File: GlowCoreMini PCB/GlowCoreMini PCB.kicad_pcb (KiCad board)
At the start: 2 copper layers, 30 x 40 mm, 62 parts, among them P1 Solder_Pad, P10 Solder_Pad, P11 Solder_Pad, P12 Solder_Pad, P13 Solder_Pad, P14 Solder_Pad, P2 Solder_Pad, P3 Solder_Pad, P4 Solder_Pad, P5 Solder_Pad, P6 Solder_Pad, P7 Solder_Pad, P8 Solder_Pad, P9 Solder_Pad, SW1 TS24CA, SW2 TS24CA, SW3 TS24CA, SW4 TS24CA, U1 ESP32-WROOM-32E, U11 AO3400A, U12 CP2102-GMR, U14 UMH3N, U2 SN74LVC2T45DCUR, U3 MSM261D4030H1CPM, U4 SN74LVC1G373DBVR, U5 AP40P05, U6 SPX3819M5-L-3-3_TR, U7 SS54, U9 SN74LVC1G373DBVR

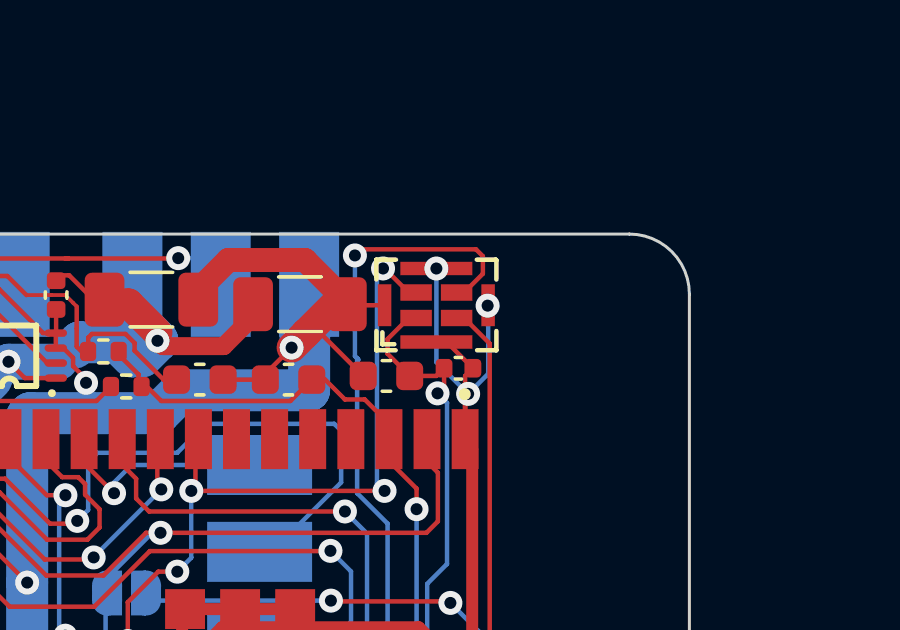
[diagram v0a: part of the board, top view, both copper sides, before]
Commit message: fixed via in ground pad
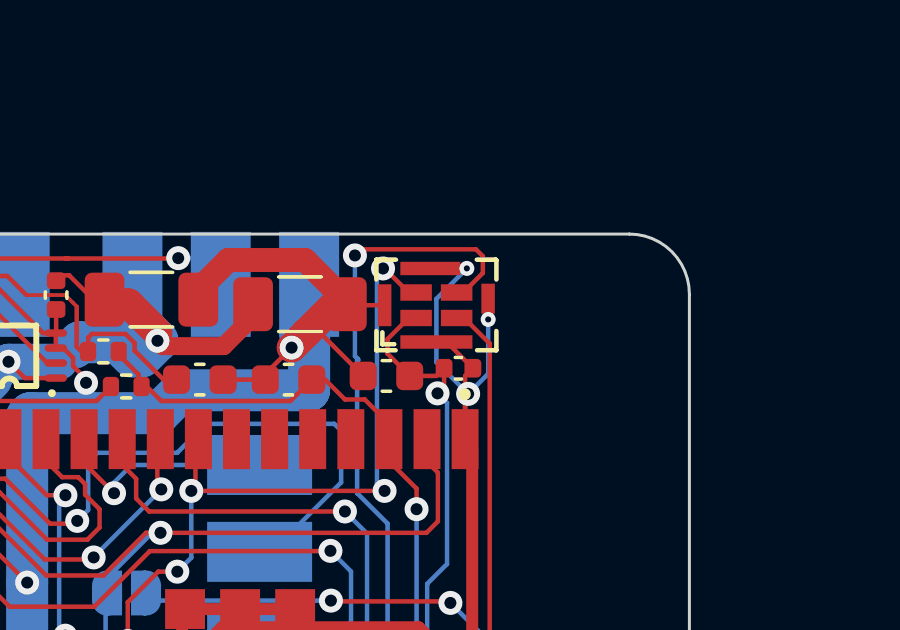
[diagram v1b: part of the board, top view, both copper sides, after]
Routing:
- net GND: track 263.4 -> 265.2 mm

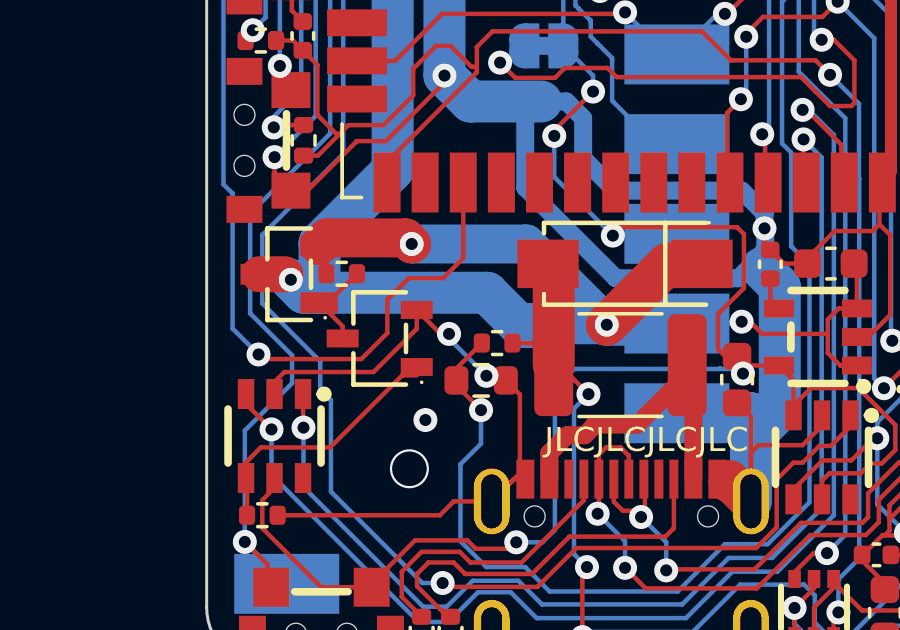
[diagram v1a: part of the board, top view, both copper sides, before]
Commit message: added status led
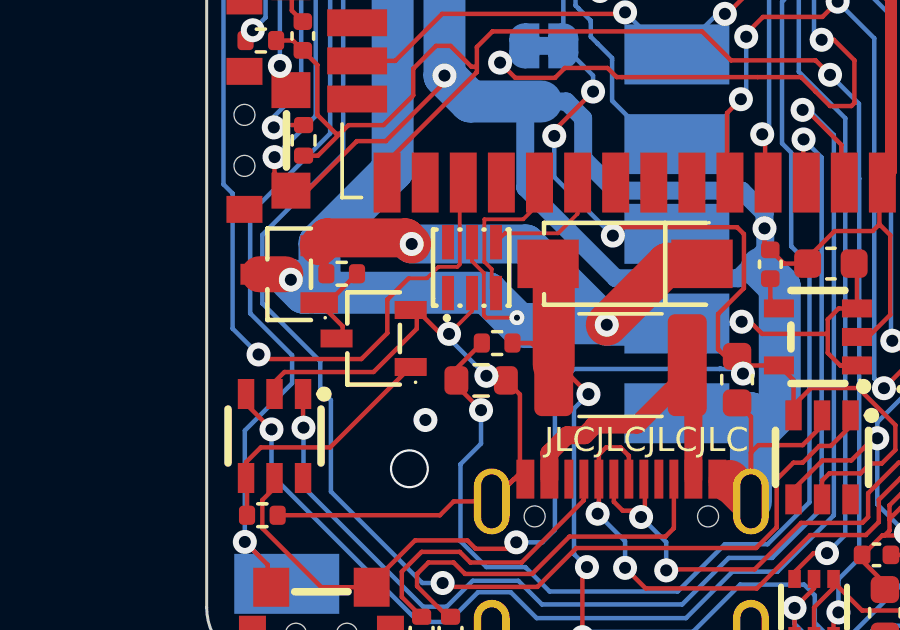
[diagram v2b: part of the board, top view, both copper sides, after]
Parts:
- added U8: SK9822-EC20, footprint:LED-SMD_6P-L2.0-W2.0-P0.80-TL, F.Cu at (91.5, 75.5)
- moved U11 0.20 mm to (88.3, 77.9)
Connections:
- U1 pad 29: IO5 -> IO5/STATUS LED DATA
- U1 pad 30: unconnected-(U1-Pad30) -> IO18/STATUS LED CLOCK
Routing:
- net IO5/STATUS LED DATA: track 0.00 -> 5.37 mm
- net IO18/STATUS LED CLOCK: track 0.00 -> 4.15 mm
- net 5V AFTER MOSFET: track 51.8 -> 55.6 mm, vias 3 -> 4
- net GND: track 265.2 -> 266.9 mm
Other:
- board text added: "Status LED: DATA: IO5 CLK: IO18"

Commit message: continued redesign of pcb
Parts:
- removed C4: 0.1uF, Capacitor_SMD:C_0402_1005Metric
- removed H1, H2: MountingHole_Pad, MountingHole:MountingHole_2.2mm_M2_ISO7380
- removed JP1: SolderJumper_2_Bridged, Jumper:SolderJumper-2_P1.3mm_Bridged_RoundedPad1.0x1.5mm
- removed JP2, JP4: SolderJumper_2_Open, Jumper:SolderJumper-2_P1.3mm_Open_RoundedPad1.0x1.5mm
- removed SW4: TS24CA, footprint:SW-SMD_TS24CA
- added C15: 10uF, Capacitor_SMD:C_0603_1608Metric, F.Cu at (88.0, 54.6)
- added C16: 0.1uF, Capacitor_SMD:C_0402_1005Metric, F.Cu at (86.1, 65.8)
- added C17: 10uF, Capacitor_SMD:C_0603_1608Metric, F.Cu at (86.1, 84.2)
- added C18: 10nF, Capacitor_SMD:C_0402_1005Metric, F.Cu at (86.4, 79.5)
- added C19: 10uF, Capacitor_SMD:C_0603_1608Metric, F.Cu at (86.3, 77.8)
- added C21: 220uF, Capacitor_SMD:C_1206_3216Metric, F.Cu at (96.7, 72.7)
- added G***: LOGO, LOGO, B.Cu at (98.0, 68.9)
- added L1: WPN4020H1R0MT, footprint:IND-SMD_L4.0-W4.0_SLW40XX, F.Cu at (99.7, 78.0)
- added P15: Solder_Pad, footprint:Solder pad, B.Cu at (99.2, 72.3)
- added P16: Solder_Pad, footprint:Solder pad, B.Cu at (95.1, 69.9)
- added P17: Solder_Pad, footprint:Solder pad, B.Cu at (99.3, 64.4)
- added P18: Solder_Pad, footprint:Solder pad, B.Cu at (99.2, 69.7)
- added P19: Solder_Pad, footprint:Solder pad, B.Cu at (95.1, 54.5)
- added P20: Solder_Pad, footprint:Solder pad, B.Cu at (99.2, 67.1)
- added P21: Solder_Pad, footprint:Solder pad, B.Cu at (95.2, 51.9)
- added P22: Solder_Pad, footprint:Solder pad, B.Cu at (99.3, 51.9)
- added R10: 10K, Resistor_SMD:R_0402_1005Metric, F.Cu at (105.1, 72.5)
- added R11: 10K, Resistor_SMD:R_0402_1005Metric, F.Cu at (104.2, 72.5)
- added R16: 100K, Resistor_SMD:R_0402_1005Metric, F.Cu at (118.8, 76.7)
- added R17: 5.1K, Resistor_SMD:R_0402_1005Metric, F.Cu at (85.8, 57.8)
- added R18: 33K, Resistor_SMD:R_0402_1005Metric, F.Cu at (87.6, 76.1)
- added R19: 100K, Resistor_SMD:R_0402_1005Metric, F.Cu at (85.5, 76.5)
- added R2: 10K, Resistor_SMD:R_0402_1005Metric, F.Cu at (89.3, 68.9)
- added R20: 10K, Resistor_SMD:R_0402_1005Metric, F.Cu at (87.7, 51.7)
- added R21: 100K, Resistor_SMD:R_0402_1005Metric, F.Cu at (92.9, 75.6)
- added R22: 100K, Resistor_SMD:R_0402_1005Metric, F.Cu at (92.9, 78.8)
- added R23: 5.1K, Resistor_SMD:R_0402_1005Metric, F.Cu at (103.7, 86.3)
- added R24: 5.1K, Resistor_SMD:R_0402_1005Metric, F.Cu at (103.7, 85.3)
- added REF1: RT9471DGQW, footprint:RT9471_vias_in_pad, F.Cu at (104.6, 76.3)
- added U10: LSM6DS3TR-C, footprint:LGA-14_L3.0-W2.5-P0.50-TL, F.Cu at (88.1, 65.8)
- added U13: SK9822-EC20, footprint:LED-SMD_6P-L2.0-W2.0-P0.80-TL, F.Cu at (96.8, 68.5)
- added U15: AP40P05, footprint:SOT-23-3_L2.9-W1.3-P1.90-LS2.4-BR, F.Cu at (94.7, 78.8)
- C1: value 0.1uF -> 1uF
- C10: value 4.7uF -> 0.1uF; footprint Capacitor_SMD:C_0603_1608Metric -> Capacitor_SMD:C_0402_1005Metric
- C12: value 10uF -> 1uF; footprint Capacitor_SMD:C_0603_1608Metric -> Capacitor_SMD:C_0402_1005Metric
- C13: value 1uF -> 0.1uF
- C14: value 10uF -> 0.1uF; footprint Capacitor_SMD:C_0603_1608Metric -> Capacitor_SMD:C_0402_1005Metric
- C2: value 0.1uF -> 10uF; footprint Capacitor_SMD:C_0402_1005Metric -> Capacitor_SMD:C_0603_1608Metric
- C5: value 10uF -> 4.7uF; footprint Capacitor_SMD:C_0603_1608Metric -> Capacitor_SMD:C_0402_1005Metric
- C6: value 10uF -> 47nF; footprint Capacitor_SMD:C_0603_1608Metric -> Capacitor_SMD:C_0402_1005Metric
- C7, C9: value 220uF -> 10uF; footprint Capacitor_SMD:C_1206_3216Metric_Pad1.33x1.80mm_HandSolder -> Capacitor_SMD:C_0603_1608Metric
- C8: value 10nF -> 10uF; footprint Capacitor_SMD:C_0402_1005Metric -> Capacitor_SMD:C_0603_1608Metric
- R1: value 62 -> 100K
- R12, R13: value 220 -> 100K
- R14, R15: value 10K -> 62
- R7, R8: value 5.1K -> 10K
- U1: value ESP32-WROOM-32E -> SN74LVC1G373DBVR; footprint footprint:WIFI-SMD_ESP32-WROOM-32E -> footprint:SOT-23-6_L2.9-W1.6-P0.95-LS2.8-BR
- U11: value AO3400A -> MSM261D4030H1CPM; footprint footprint:SOT-23-3_L2.9-W1.6-P1.90-LS2.8-BR -> footprint:MIC-SMD_8P-L4.0-W3.0_ZTS6231
- U12: value CP2102-GMR -> SPX3819M5-L-3-3_TR; footprint footprint:QFN-28_L5.0-W5.0-P0.50-BL-EP -> footprint:SOT-23-5_L3.0-W1.7-P0.95-LS2.8-BR
- U14: value UMH3N -> AP40P05; footprint footprint:SC-70-6_L2.2-W1.3-P0.65-LS2.1-BR -> footprint:SOT-23-3_L2.9-W1.3-P1.90-LS2.4-BR
- U2: value SN74LVC2T45DCUR -> ESP32-S3-MINI-1-N8; footprint footprint:VSSOP-8_L2.4-W2.1-P0.50-LS3.2-BR -> footprint:ESP32-S3-MINI-1-N8
- U3: value MSM261D4030H1CPM -> PTVSHC3N12VU; footprint footprint:MIC-SMD_8P-L3.0-W4.0-P0.85-BL -> footprint:DFN-3_L2.0-W2.0-P1.30-BR
- U4: value SN74LVC1G373DBVR -> AP40P05; footprint footprint:SOT-23-6_L2.9-W1.6-P0.95-LS2.8-BR -> footprint:SOT-23-3_L2.9-W1.3-P1.90-LS2.4-BR
- U6: value SPX3819M5-L-3-3_TR -> AO3400A; footprint footprint:SOT-23-5_L3.0-W1.7-P0.95-LS2.8-BR -> footprint:SOT-23-3_L2.9-W1.6-P1.90-LS2.8-BR
- U7: value SS54 -> 74LVC2G04DW-7; footprint footprint:SMA_L4.4-W2.8-LS5.4-RD -> footprint:SOT-363_L2.0-W1.3-P0.65-LS2.1-BR
- U8: value SK9822-EC20 -> AP40P05; footprint footprint:LED-SMD_6P-L2.0-W2.0-P0.80-TL -> footprint:SOT-23-3_L2.9-W1.3-P1.90-LS2.4-BR
- U9: value SN74LVC1G373DBVR -> SN74LVC2T45DCUR; footprint footprint:SOT-23-6_L2.9-W1.6-P0.95-LS2.8-BR -> footprint:VSSOP-8_L2.4-W2.1-P0.50-LS3.2-BR
- moved SW2 38.7 mm to (107.5, 87.8), turned to 180 degrees
- moved R9 37.6 mm to (118.8, 77.7)
- moved C2 33.2 mm to (106.2, 80.5)
- moved C1 30.7 mm to (107.8, 76.9)
- moved R1 28.9 mm to (107.4, 73.6), turned to 0 degrees
- moved U3 28.1 mm to (108.6, 78.9), turned to 0 degrees
- moved C11 27.7 mm to (85.2, 65.8), turned to -90 degrees
- moved C5 26.5 mm to (104.8, 79.9), turned to -90 degrees
- moved P1 26.0 mm to (95.1, 76.5), turned to -90 degrees
- moved P13 26.0 mm to (95.2, 62.1), turned to 90 degrees
- moved P2 26.0 mm to (99.2, 76.5), turned to -90 degrees
- moved C9 23.5 mm to (100.2, 73.9), turned to -90 degrees
- moved P3 22.5 mm to (95.1, 72.5), turned to -90 degrees
- moved U12 22.5 mm to (86.4, 81.5)
- moved C7 21.8 mm to (101.7, 72.9), turned to -90 degrees
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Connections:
- C1 pad 1: 5V AFTER MOSFET -> -BATT
- C1 pad 2: GND -> VBUS
- C10 pad 1: GND -> 5V AFTER MOSFET
- C10 pad 2: Net-(C10-Pad2) -> -BATT
- C11 pad 1: Net-(C10-Pad2) -> 3.3V AFTER MOSFET
- C11 pad 2: GND -> -BATT
- C12 pad 1: GND -> -BATT
- C13 pad 1: IO0 -> -BATT
- C13 pad 2: GND -> 3.3V AFTER MOSFET
- C14 pad 1: GND -> 3.3V AFTER MOSFET
- C14 pad 2: +3V3 -> -BATT
- C2 pad 1: +3V3 -> -BATT
- C2 pad 2: GND -> Net-(REF1-PMID)
- C3 pad 1: +3V3 -> -BATT
- C3 pad 2: GND -> +3V3
- C5 pad 1: GND -> REGN
- C5 pad 2: Net-(C4-Pad2) -> -BATT
- C6 pad 1: GND -> Net-(REF1-BTST)
- C6 pad 2: +5V -> Net-(C6-Pad2)
- C7 pad 1: 5V AFTER MOSFET -> -BATT
- C7 pad 2: GND -> +BATT
- C8 pad 1: GND -> -BATT
- C8 pad 2: Net-(C8-Pad2) -> +5V
- C9 pad 1: 5V AFTER MOSFET -> -BATT
- C9 pad 2: GND -> +5V
- F1 pad 1: Net-(F1-Pad1) -> +5V
- F1 pad 2: VBUS -> Net-(F1-Pad2)
- P1 pad 1: 5V AFTER MOSFET -> Net-(U8-D)
- P10 pad 1: +3V3 -> 3.3V AFTER MOSFET
- P11 pad 1: IO32/SD -> EN
- P12 pad 1: IO27 -> LED1 DATA OUT
- P13 pad 1: IO33/MAINBUTTON -> IO1/POWERBUTTON
- P14 pad 1: IO26 -> IO3/ACTIONBUTTON
- P2 pad 1: LED1 DATA OUT -> -BATT
- P3 pad 1: GND -> 5V AFTER MOSFET
- P4 pad 1: +5V -> Net-(F1-Pad2)
- P5 pad 1: GND -> -BATT
- P6 pad 1: IO12/TDI -> IO36/SPI SCK
- P7 pad 1: IO13/TCK -> IO35/SPI MO
- P8 pad 1: IO14/SCK/TMS -> TXD0
- P9 pad 1: IO15/WS/TDO -> RXD0
- R1 pad 1: Net-(R1-Pad1) -> IO47/BATT IC EN
- R1 pad 2: LED1 DATA OUT -> -BATT
- R12 pad 1: Net-(R12-Pad1) -> Net-(U14-G)
- R12 pad 2: EN -> +3V3
- R13 pad 1: Net-(R13-Pad1) -> -BATT
- R13 pad 2: IO0 -> Net-(U8-G)
- R14 pad 1: EN -> Net-(U9-A1)
- R14 pad 2: +3V3 -> LED1 DATA OUT
- R15 pad 1: IO0 -> Net-(U9-A2)
- R15 pad 2: +3V3 -> LED2 DATA OUT
- R3 pad 1: IO25/VBUS -> IO7/VBUS
- R4 pad 1: GND -> -BATT
- R4 pad 2: IO25/VBUS -> IO7/VBUS
- R5 pad 1: Net-(R5-Pad1) -> Net-(U14-G)
- R6 pad 1: GND -> -BATT
- R6 pad 2: Net-(R6-Pad2) -> Net-(U1-Q)
- R7 pad 1: GND -> +3V3
- R7 pad 2: USB-C CC1 -> IO9/I2C SCL
- R8 pad 1: GND -> +3V3
- R8 pad 2: USB-C CC2 -> IO10/I2C GRYO INT
- R9 pad 1: Net-(R9-Pad1) -> Net-(U7-1A)
- R9 pad 2: GND -> +3V3
- SW1 pad 3: +3V3 -> -BATT
- SW1 pad 4: IO33/MAINBUTTON -> Net-(U7-1A)
- SW2 pad 3: Net-(R9-Pad1) -> -BATT
- SW2 pad 4: +3V3 -> IO0/BOOT
- SW3 pad 3: GND -> -BATT
- SW3 pad 4: Net-(R12-Pad1) -> EN
- U1 pad 1: GND -> IO15/LED LETCH EN
- U1 pad 2: +3V3 -> -BATT
- U1 pad 3: EN -> IO16/POWERMOSFETS
- U1 pad 4: unconnected-(U1-Pad4) -> Net-(U1-Q)
- U1 pad 5: unconnected-(U1-Pad5) -> +3V3
- U11 pad 1: Net-(R6-Pad2) -> 3.3V AFTER MOSFET
- U11 pad 2: GND -> IO12/I2S WS
- U11 pad 3: Net-(R5-Pad1) -> IO13/I2S SCK
- U12 pad 1: unconnected-(U12-Pad1) -> +5V
- U12 pad 2: unconnected-(U12-Pad2) -> -BATT
- U12 pad 3: GND -> +5V
- U12 pad 4: USB-C DATA+ -> Net-(U12-BYP)
- U12 pad 5: USB-C DATA- -> +3V3
- U14 pad 1: RTS -> Net-(U14-G)
- U14 pad 2: DTR -> +5V
- U14 pad 3: IO0 -> 5V AFTER MOSFET
- U2 pad 1: 5V AFTER MOSFET -> -BATT
- U2 pad 2: Net-(R1-Pad1) -> -BATT
- U2 pad 3: GND -> +3V3
- U2 pad 4: GND -> IO0/BOOT
- U2 pad 5: GND -> IO1/POWERBUTTON
- U2 pad 6: GND -> IO2/BATT VOLT
- U2 pad 7: IO16/LED1 -> IO3/ACTIONBUTTON
- U2 pad 8: +3V3 -> unconnected-(U2-IO4-Pad8)
- U3 pad 1: Net-(C4-Pad2) -> -BATT
- U3 pad 2: IO15/WS/TDO -> -BATT
- U3 pad 3: IO14/SCK/TMS -> VBUS
- U4 pad 1: IO22/LED LETCH EN -> Net-(U14-G)
- U4 pad 2: GND -> +5V
- U4 pad 3: IO23/POWERMOSFETS -> 5V AFTER MOSFET
- U5 pad 1: Net-(R5-Pad1) -> Net-(U14-G)
- U5 pad 2: +5V -> +3V3
- U5 pad 3: 5V AFTER MOSFET -> 3.3V AFTER MOSFET
- U6 pad 1: +5V -> Net-(U1-Q)
- U6 pad 2: GND -> -BATT
- U6 pad 3: +5V -> Net-(U14-G)
- U7 pad 1: +5V -> Net-(U7-1A)
- U7 pad 2: VBUS -> -BATT
- U8 pad 1: unconnected-(U8-Pad1) -> Net-(U8-G)
- U8 pad 2: GND -> +BATT
- U8 pad 3: IO5/STATUS LED DATA -> Net-(U8-D)
- U9 pad 1: Net-(R9-Pad1) -> 5V AFTER MOSFET
- U9 pad 2: GND -> Net-(U9-A1)
- U9 pad 3: +3V3 -> Net-(U9-A2)
- U9 pad 4: Net-(C10-Pad2) -> -BATT
- U9 pad 5: +3V3 -> -BATT
- U9 pad 6: unconnected-(U9-Pad6) -> IO41/LED2
- USB1 pad A1B12: GND -> -BATT
- USB1 pad A4B9: Net-(F1-Pad1) -> VBUS
- USB1 pad A6: USB-C DATA+ -> USB D+
- USB1 pad A7: USB-C DATA- -> USB D-
- USB1 pad B1A12: GND -> -BATT
- USB1 pad B4A9: Net-(F1-Pad1) -> VBUS
- USB1 pad B6: USB-C DATA+ -> USB D+
- USB1 pad B7: USB-C DATA- -> USB D-
- USB1 pad SHELL: GND -> -BATT
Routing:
- net GND: track 266.9 -> 0.00 mm, vias 18 -> 0
- net +3V3: track 133.7 -> 0.00 mm, vias 10 -> 0
- net Net-(R9-Pad1): track 64.5 -> 0.00 mm, vias 2 -> 0
- net IO25/VBUS: track 56.5 -> 0.00 mm, vias 2 -> 0
- net 5V AFTER MOSFET: track 55.6 -> 0.00 mm, vias 4 -> 0
- net IO0: track 50.3 -> 0.00 mm, vias 2 -> 0
- net IO14/SCK/TMS: track 48.5 -> 0.00 mm, vias 6 -> 0
- net IO33/MAINBUTTON: track 47.0 -> 0.00 mm, vias 4 -> 0
- net Net-(C10-Pad2): track 44.7 -> 0.00 mm, vias 4 -> 0
- net EN: track 43.6 -> 0.00 mm, vias 2 -> 0
- net IO23/POWERMOSFETS: track 43.1 -> 0.00 mm, vias 2 -> 0
- net IO16/LED1: track 41.2 -> 0.00 mm, vias 2 -> 0
- net IO22/LED LETCH EN: track 38.0 -> 0.00 mm, vias 2 -> 0
- net Net-(C4-Pad2): track 36.2 -> 0.00 mm, vias 3 -> 0
- net IO15/WS/TDO: track 35.5 -> 0.00 mm, vias 4 -> 0
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- added copper zone on In2.Cu, net +5V
- added copper zone on In1.Cu, net -BATT
- added copper zone on In2.Cu, net 5V AFTER MOSFET
- removed copper zone on B.Cu, net GND
- removed copper zone on F.Cu, net GND
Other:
- outline, holes or cut-outs redrawn
- copper layers 2 -> 4
- board text removed: "200mA max"
- board text removed: "2A max"
- board text removed: "3.3V OUT"
- board text removed: "3A max"
- board text removed: "5V"
- board text removed: "5V IN"
- board text removed: "BOOT"
- board text removed: "G"
- board text removed: "GND"
- board text removed: "GlowCore Mini v2.0"
- board text removed: "IO12/TDI"
- board text removed: "IO13/TCK"
- board text removed: "IO14/SCK/TMS"
- board text removed: "IO15/WS/TDO"
- board text removed: "IO16"
- board text removed: "IO26"
- board text removed: "IO27"
- board text removed: "IO32/SD"
- board text removed: "IO33/ B1"
- board text removed: "LEDs always on"
- board text removed: "RESET"
- board text removed: "SERIAL"
- board text removed: "Serial always on"
- board text removed: "Status LED: DATA: IO5 CLK: IO18"
- board text removed: "https:// bit.ly/ 3GnbIkg"
- board text removed: "microphone on"

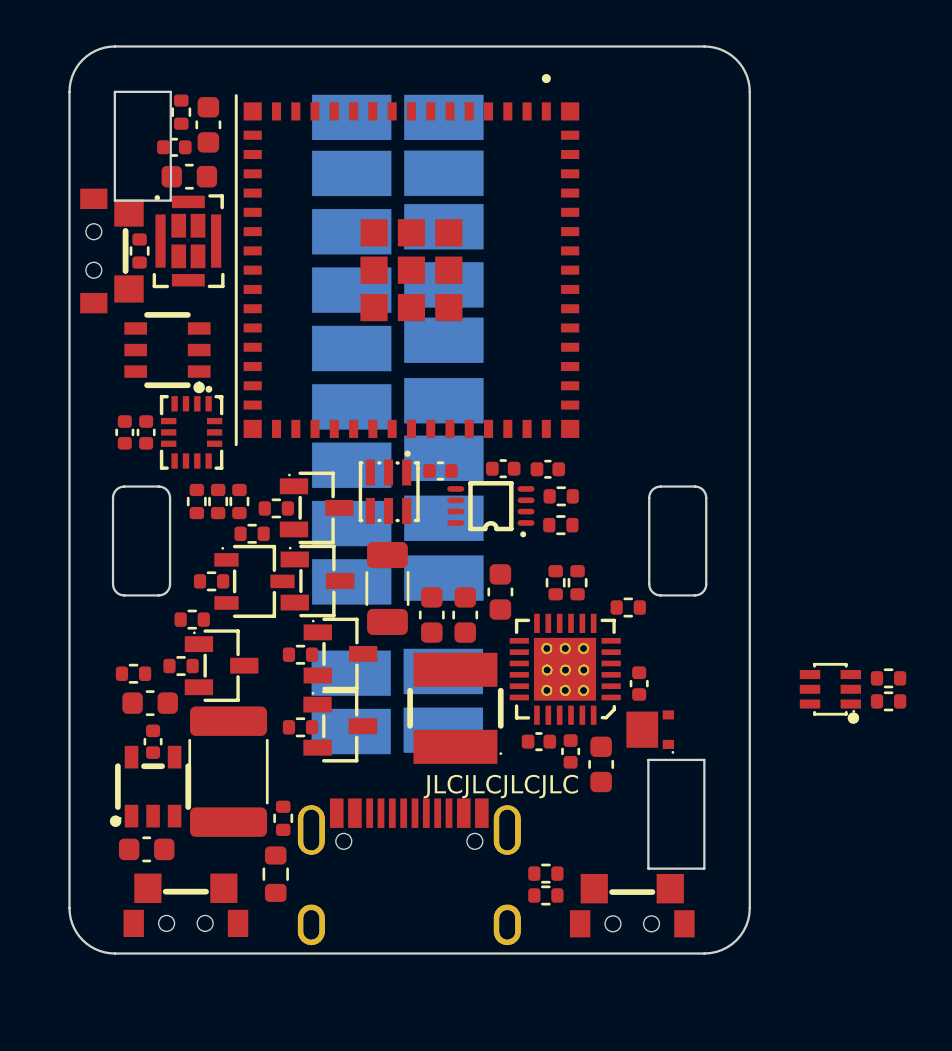
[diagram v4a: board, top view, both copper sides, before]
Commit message: split up schematic
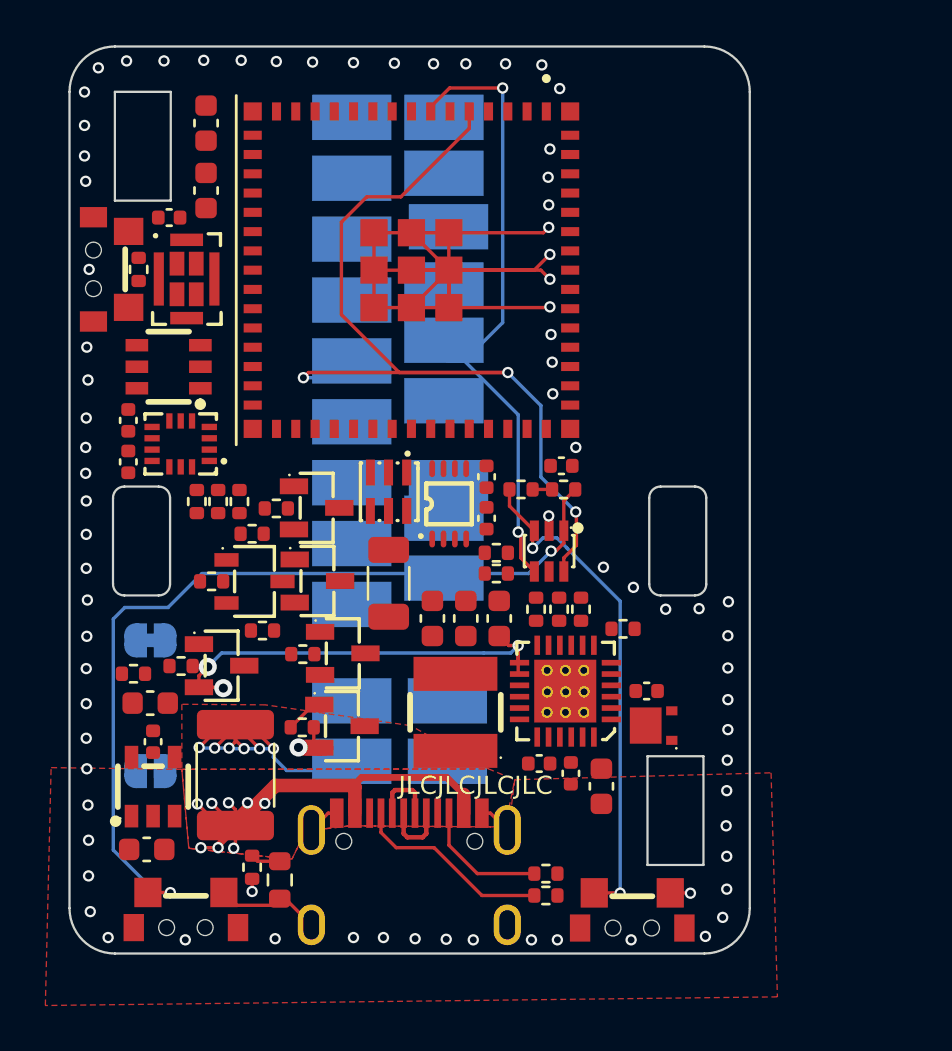
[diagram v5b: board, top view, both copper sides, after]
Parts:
- removed G***: LOGO, LOGO
- added JP1: SolderJumper_2_Open, Jumper:SolderJumper-2_P1.3mm_Open_RoundedPad1.0x1.5mm, B.Cu at (86.3, 80.8)
- added JP2: SolderJumper_2_Bridged, Jumper:SolderJumper-2_P1.3mm_Bridged_RoundedPad1.0x1.5mm, B.Cu at (86.3, 75.0)
- moved R20 26.9 mm to (103.3, 73.6), turned to -90 degrees
- moved R16 18.2 mm to (102.6, 68.4)
- moved R9 17.1 mm to (104.5, 68.4), turned to 180 degrees
- moved U7 13.8 mm to (103.9, 71.1), turned to 90 degrees
- moved R15 3.79 mm to (101.5, 71.1)
- moved R14 3.56 mm to (101.5, 72.1)
- moved R13 3.14 mm to (91.2, 74.6)
- moved C13 3.11 mm to (87.1, 56.4)
- moved R3 2.56 mm to (90.8, 85.0), turned to -90 degrees
- moved C10 2.31 mm to (101.1, 69.6), turned to -90 degrees
- moved C14 2.05 mm to (101.1, 67.8), turned to -90 degrees
- moved U9 1.85 mm to (99.5, 69.0), turned to -90 degrees
- moved U11 1.67 mm to (87.9, 59.1)
- moved P2 1.38 mm to (99.3, 77.8)
- moved P5 1.38 mm to (99.3, 80.4)
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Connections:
- C17 pad 2: +5V -> VSYS
- C21 pad 1: +5V -> VBUS
- C8 pad 2: +5V -> Net-(JP2-A)
- C9 pad 2: +5V -> Net-(JP2-A)
- F1 pad 1: +5V -> Net-(JP1-A)
- F1 pad 2: Net-(F1-Pad2) -> VBUS
- L1 pad 2: +5V -> Net-(JP2-A)
- P4 pad 1: Net-(F1-Pad2) -> VBUS
- R21 pad 2: +5V -> VBUS
- R22 pad 2: +5V -> VBUS
- R5 pad 2: +5V -> VBUS
- REF1 pad 15: +5V -> Net-(JP2-A)
- REF1 pad 16: +5V -> Net-(JP2-A)
- U12 pad 1: +5V -> VSYS
- U12 pad 3: +5V -> VSYS
- U14 pad 2: +5V -> VBUS
- U15 pad 2: +5V -> VBUS
- U4 pad 2: +5V -> VBUS
- USB1 pad A4B9: VBUS -> Net-(JP1-A)
- USB1 pad B4A9: VBUS -> Net-(JP1-A)
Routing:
- net -BATT: track 0.00 -> 51.9 mm, vias 0 -> 75
- net IO1/POWERBUTTON: track 0.00 -> 42.4 mm, vias 0 -> 3
- net Net-(U7-1A): track 0.00 -> 38.3 mm, vias 0 -> 2
- net IO3/ACTIONBUTTON: track 0.00 -> 27.9 mm, vias 0 -> 2
- net Net-(JP1-A): track 0.00 -> 25.2 mm, vias 0 -> 8
- net IO0/BOOT: track 0.00 -> 22.3 mm, vias 0 -> 2
- net +BATT: track 0.00 -> 20.0 mm, vias 0 -> 3
- net VBUS: track 0.00 -> 19.7 mm, vias 0 -> 8
- net USB-C CC1: track 0.00 -> 8.76 mm
- net USB-C CC2: track 0.00 -> 5.69 mm
- net USB D+: track 0.00 -> 2.94 mm
- net USB D-: track 0.00 -> 2.90 mm
- net Net-(U14-G): track 0.00 -> 1.68 mm
- net IO7/VBUS: track 0.00 -> 1.32 mm
- net +3V3: track 0.00 -> 0.86 mm
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- added copper zone on F.Cu, net -BATT
- added copper zone on F.Cu, net Net-(JP1-A)
- added copper zone on F.Cu, net VBUS
- added copper zone on In2.Cu, net VBUS
- removed copper zone on In2.Cu, net +5V
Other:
- outline, holes or cut-outs redrawn
- board text added: "AB"
- board text added: "EN"
- board text added: "GlowCore Mini v3.1"
- board text added: "PB"
- board text added: "bit.ly/ 3l6y4On"
- board text added: "locked"

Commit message: updated pcb design
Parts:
- moved P15 1.19 mm to (99.4, 73.5)
- moved P18 1.13 mm to (99.3, 70.8)
- moved P17 0.95 mm to (99.4, 65.3)
- moved P14 0.92 mm to (99.4, 62.6)
- moved P9 0.69 mm to (99.2, 60.1)
- moved P7 0.59 mm to (99.2, 57.4)
- moved R10 0.49 mm to (105.8, 73.6), turned to 180 degrees
- moved P6 0.23 mm to (99.3, 54.6)
- moved C4 0.10 mm to (96.8, 72.6)
- moved JP2 0.05 mm to (86.3, 75.1)
- turned C13 to 180 degrees
- turned C14 to 90 degrees
- turned R17 to 90 degrees
- turned R22 to 180 degrees
- renumbered C21 to C4, U5 to U15, U15 to U5
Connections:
- R22 pad 1: Net-(U14-G) -> VBUS
- R22 pad 2: VBUS -> Net-(U14-G)
- U2 pad 37: IO41/LED2 -> IO41/LED1
- U2 pad 38: IO42/LED1 -> IO42/LED2
- U9 pad 6: IO41/LED2 -> IO42/LED2
- U9 pad 7: IO42/LED1 -> IO41/LED1
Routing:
- net +3V3: track 0.86 -> 101.5 mm, vias 0 -> 14
- net 3.3V AFTER MOSFET: track 0.00 -> 65.9 mm, vias 0 -> 7
- net IO8/I2C SDA: track 0.00 -> 60.5 mm, vias 0 -> 4
- net IO9/I2C SCL: track 0.00 -> 53.3 mm, vias 0 -> 5
- net IO7/VBUS: track 1.32 -> 53.5 mm, vias 0 -> 2
- net -BATT: track 51.9 -> 98.6 mm, vias 75 -> 99
- net IO2/BATT VOLT: track 0.00 -> 43.1 mm, vias 0 -> 2
- net IO11/I2C BATT IC INT: track 0.00 -> 41.9 mm, vias 0 -> 3
- net EN: track 0.00 -> 36.8 mm, vias 0 -> 4
- net USB D-: track 2.90 -> 36.7 mm, vias 0 -> 2
- net USB D+: track 2.94 -> 36.2 mm, vias 0 -> 2
- net IO47/BATT IC EN: track 0.00 -> 31.4 mm, vias 0 -> 2
- net Net-(JP2-A): track 0.00 -> 29.9 mm, vias 0 -> 4
- net IO0/BOOT: track 22.3 -> 48.9 mm, vias 2 -> 3
- net IO35/SPI MO: track 0.00 -> 26.0 mm, vias 0 -> 1
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- added copper zone on B.Cu, net +BATT
- added copper zone on F.Cu, net +BATT
- added copper zone on B.Cu, net -BATT
- added copper zone on F.Cu, net 3.3V AFTER MOSFET
- added copper zone on B.Cu, net 5V AFTER MOSFET
- added copper zone on F.Cu, net 5V AFTER MOSFET
- added copper zone on F.Cu, net Net-(C6-Pad2)
- added copper zone on B.Cu, net Net-(JP1-A)
- added copper zone on B.Cu, net Net-(JP2-A)
- added copper zone on F.Cu, net Net-(JP2-A)
- added copper zone on B.Cu, net Net-(U8-D)
- added copper zone on F.Cu, net Net-(U8-D)
- added copper zone on B.Cu, net VBUS
- added copper zone on B.Cu, net VSYS
- added copper zone on F.Cu, net VSYS
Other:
- outline, holes or cut-outs redrawn

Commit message: updated pcb
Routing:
- net -BATT: track 98.6 -> 101.0 mm
- net Net-(JP1-A): track 27.2 -> 27.8 mm
- removed copper zone on B.Cu, net Net-(JP2-A)
